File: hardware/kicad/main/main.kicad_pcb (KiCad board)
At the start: 2 copper layers, 44 x 68 mm, 60 parts, among them J1 USB_C_Receptacle_USB2.0, J10 ENC_LEFT, J11 ENC_RIGHT, J12 UART0, J2 SERVO_L, J3 SERVO_R, J4 BAT, J8 Conn_02x10_Odd_Even, Q1 2N7002K, SW1 SW_SPST, SW2 SW_SPST, SW3 SW_SPST, SW4 SW_SPST, U2 AP1117-33, U5 IP5306, U6 ESP32-S3-WROOM-1

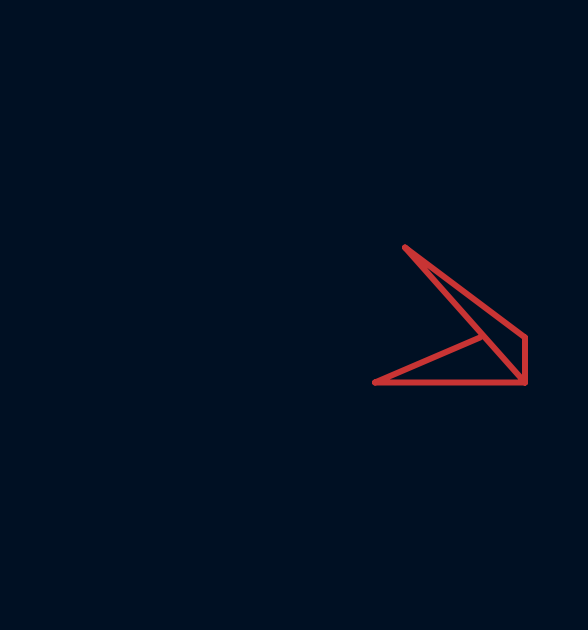
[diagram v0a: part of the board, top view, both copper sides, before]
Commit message: added interactive bom, updated blend files with more clearance on 18650 cell
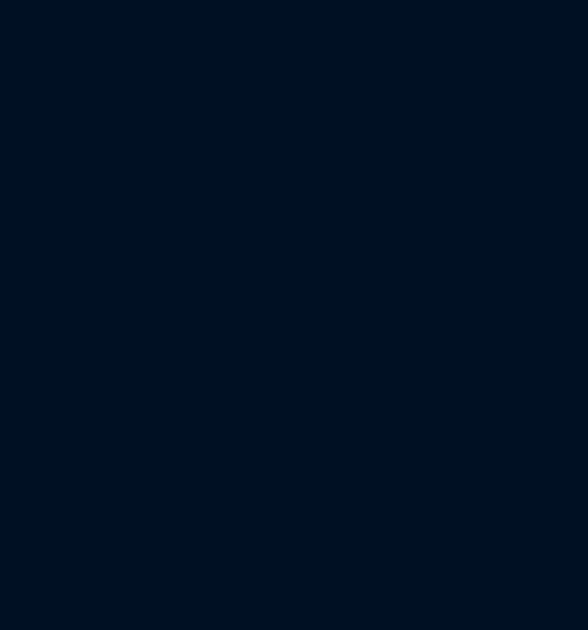
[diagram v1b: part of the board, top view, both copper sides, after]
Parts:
- J8: value Conn_02x10_Odd_Even -> EXPANSION
